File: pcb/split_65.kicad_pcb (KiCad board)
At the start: 2 copper layers, 375 x 105.4 mm, 333 parts, among them J1 PJ-3200B-4A, J10 AVR-ISP-6, J11 Breakaway_Tabs, J12 Breakaway_Tabs, J13 Breakaway_Tabs, J14 Breakaway_Tabs, J15 Breakaway_Tabs, J16 Breakaway_Tabs, J2 AVR-ISP-6, J3 Breakaway_Tabs, J4 Breakaway_Tabs, J5 Breakaway_Tabs, J6 Breakaway_Tabs, J7 Breakaway_Tabs, J8 Breakaway_Tabs, J9 PJ-3200B-4A, Q1 2N7002, Q2 2N7002, SW1 SW_Push, SW2 SW_Push, U1 ATmega32U4-AU, U2 PRTR5V0U2X, U3 ATmega32U4-AU, U4 PRTR5V0U2X, Y1 16MHz, Y2 16MHz

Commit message: moved usb/trrs port closer in
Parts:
- moved USB1 2.08 mm to (61.9, 44.4)
- moved USB2 2.08 mm to (340.5, 44.4)
- moved J1 2.08 mm to (138.1, 46.1)
- moved J9 2.08 mm to (264.3, 46.1)
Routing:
- net GND: track 71.9 -> 47.2 mm
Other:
- board size 375 x 105.4 mm -> 375 x 103.3 mm

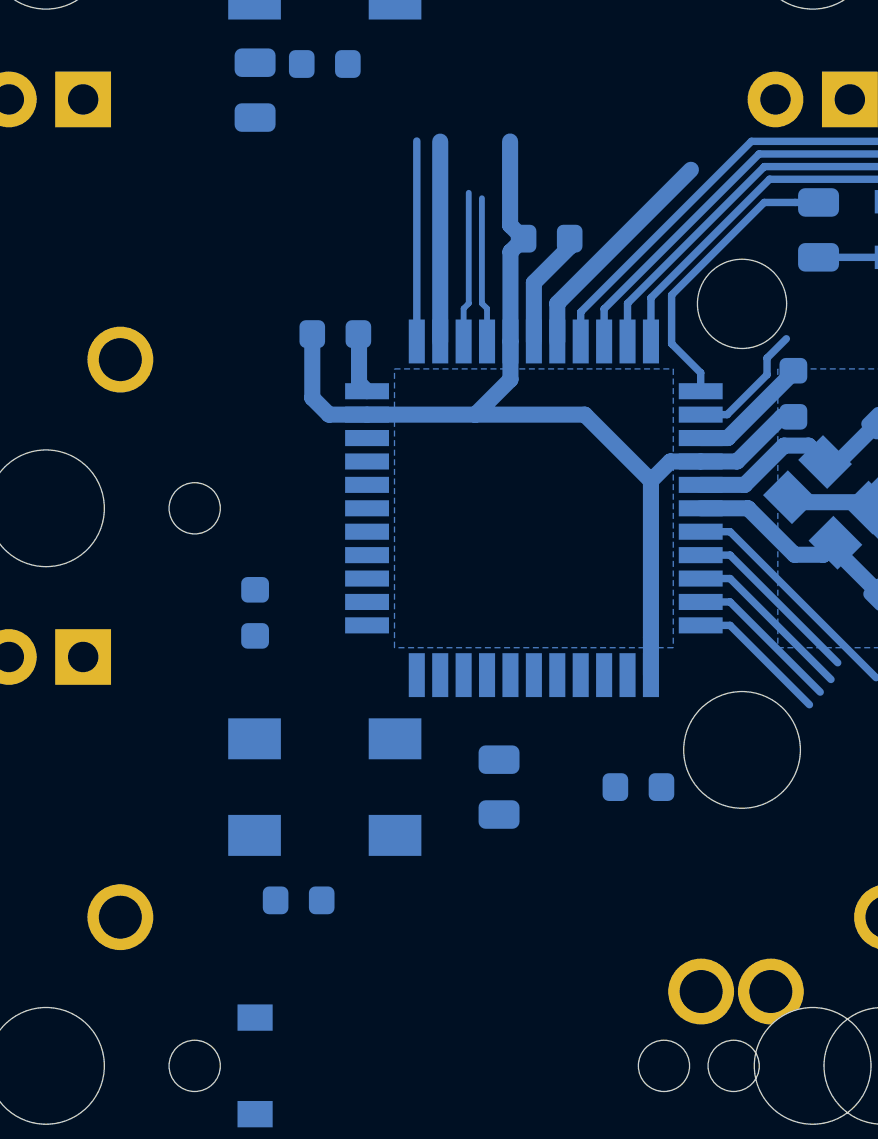
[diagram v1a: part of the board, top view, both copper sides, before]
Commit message: break out mcu pins
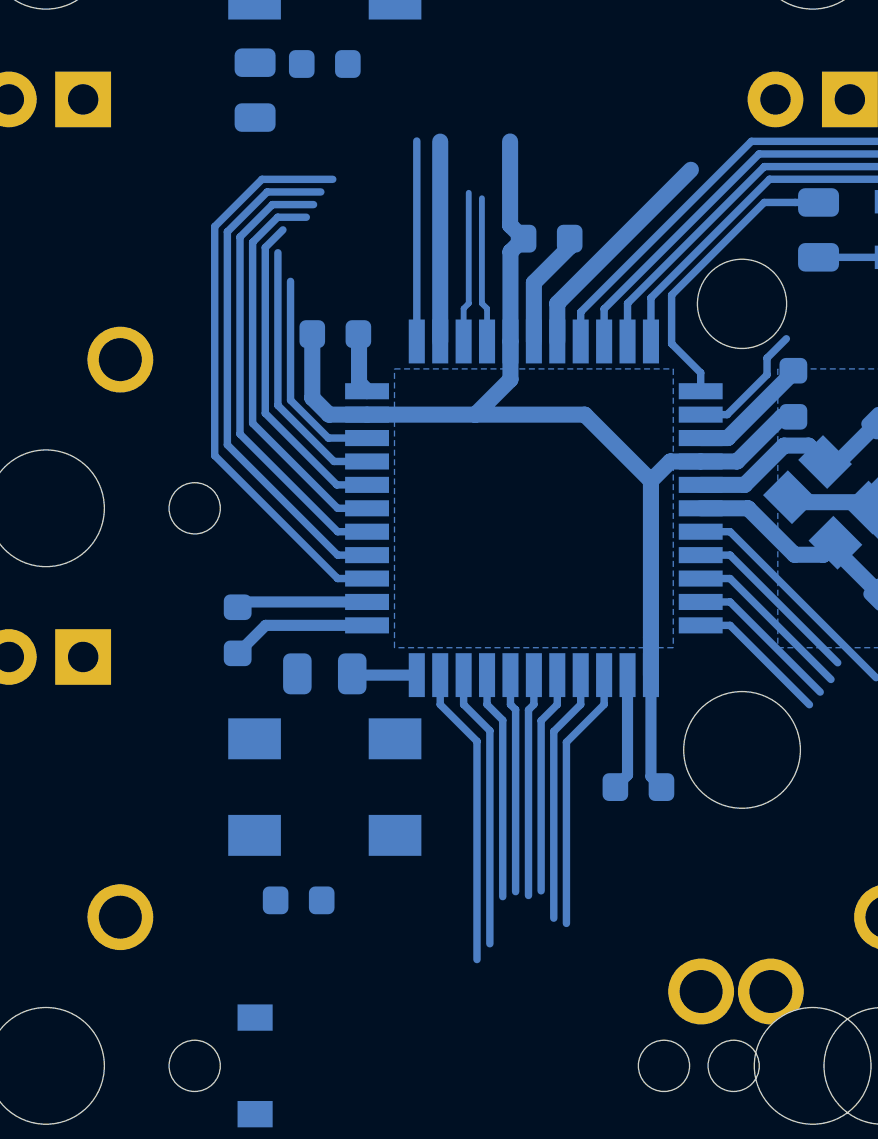
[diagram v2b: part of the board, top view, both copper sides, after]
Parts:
- moved R24 7.10 mm to (38.1, 124.7), turned to 0 degrees
- moved C6 0.84 mm to (35.1, 123.2)
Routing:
- net ROW0: track 0.00 -> 19.5 mm
- net ROW1: track 0.00 -> 17.4 mm
- net ROW2: track 0.00 -> 15.4 mm
- net ROW3: track 0.00 -> 13.5 mm
- net COL5: track 0.00 -> 11.0 mm
- net COL0: track 0.00 -> 10.2 mm
- net Net-(U1-Pad31): track 0.00 -> 9.55 mm
- net COL6: track 0.00 -> 9.05 mm
- net COL4: track 0.00 -> 9.02 mm
- net +5V: track 6.23 -> 15.0 mm
- net COL3: track 0.00 -> 8.69 mm
- net GND: track 47.2 -> 55.7 mm
- net Net-(U1-Pad30): track 0.00 -> 7.79 mm
- net COL1: track 0.00 -> 7.60 mm
- net COL2: track 0.00 -> 7.60 mm
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
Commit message: added more renders, changed pcb layout
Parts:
- added R91: 470, Resistor_SMD:R_0805_2012Metric, F.Cu at (168.0, -12.5)
- added R92: 470, Resistor_SMD:R_0805_2012Metric, F.Cu at (169.3, -14.8)
- C1, C10, C11, C12, C13, C14, C15, C16, C17, C18, C19, C2, C20, C21, C22, C23, C24, C25, C26, C27, C28, C29, C3, C30, C4, C5, C6, C7, C8, C9, D0, D1, D10, D11, D12, D13, D14, D15, D16, D17, D18, D19, D2, D20, D21, D22, D23, D24, D25, D26, D27, D28, D29, D3, D30, D31, D32, D33, D34, D35, D36, D37, D38, D39, D4, D40, D41, D42, D43, D44, D45, D46, D47, D48, D49, D5, D50, D51, D52, D53, D54, D55, D56, D57, D58, D59, D6, D60, D61, D62, D63, D64, D65, D66, D67, D68, D69, D7, D70, D71, D72, D73, D74, D75, D76, D8, D9, F1, F2, FID1, FID2, FID3, FID4, FID5, FID6, J10, J11, J12, J13, J14, J15, J16, J2, J3, J4, J5, J6, J7, J8, Q1, Q2, R0, R1, R10, R11, R12, R13, R14, R15, R16, R17, R18, R19, R2, R20, R21, R22, R23, R24, R25, R26, R27, R28, R29, R3, R30, R31, R32, R33, R34, R35, R36, R37, R38, R39, R4, R40, R41, R42, R43, R44, R45, R46, R47, R48, R49, R5, R50, R51, R52, R53, R54, R55, R56, R57, R58, R59, R6, R60, R61, R62, R63, R64, R65, R66, R67, R68, R69, R7, R70, R71, R72, R73, R74, R75, R76, R77, R78, R79, R8, R80, R81, R82, R83, R84, R85, R86, R87, R88, R89, R9, R90, SW1, SW2, U1, U2, U3, U4, Y1, Y2: moved to F.Cu
- LED1, LED10, LED11, LED12, LED13, LED14, LED15, LED16, LED2, LED3, LED4, LED5, LED6, LED7, LED8, LED9: value VAL** -> WS2812B; moved to F.Cu
- MX0, MX1, MX10, MX11, MX12, MX13, MX14, MX15, MX18, MX19, MX2, MX20, MX21, MX22, MX23, MX25, MX26, MX27, MX28, MX29, MX3, MX30, MX38, MX39, MX4, MX40, MX41, MX42, MX43, MX44, MX46, MX47, MX48, MX49, MX5, MX50, MX51, MX52, MX53, MX54, MX56, MX57, MX58, MX59, MX6, MX60, MX61, MX62, MX64, MX65, MX66, MX67, MX68, MX69, MX7, MX71, MX72, MX8, MX80, MX81, MX82: value 1U -> MXOnly-1U
- MX31: footprint MX_Alps_Hybrid:MXOnly-1.5U-FLIPPED -> MX_Alps_Hybrid:MXOnly-1U
- MX33, MX35: footprint MX_Alps_Hybrid:MXOnly-1.25U -> MX_Alps_Hybrid:MXOnly-1.25U-FLIPPED
- MX34: footprint MX_Alps_Hybrid:MXOnly-1.5U -> MX_Alps_Hybrid:MXOnly-1.25U
- moved J13 420.1 mm to (54.9, -96.0), turned to 0 degrees
- moved R89 418.4 mm to (298.0, -141.3), turned to 0 degrees
- moved J3 414.0 mm to (11.9, -11.7), turned to 0 degrees
- moved J7 404.6 mm to (17.7, -11.7), turned to 0 degrees
- moved J14 400.5 mm to (11.9, -12.6), turned to 0 degrees
- moved J8 399.4 mm to (17.7, -10.8), turned to 0 degrees
- moved J12 389.6 mm to (11.9, -10.8), turned to 0 degrees
- moved SW2 389.1 mm to (13.2, -15.9), turned to 0 degrees
- moved J11 385.5 mm to (23.6, -10.7), turned to 0 degrees
- moved D22 377.8 mm to (293.9, -142.6), turned to 0 degrees
- moved J15 372.6 mm to (66.6, -96.0), turned to 0 degrees
- moved J16 372.6 mm to (60.7, -96.0), turned to 0 degrees
- moved R40 371.8 mm to (263.3, -99.3), turned to 0 degrees
- moved C30 370.0 mm to (38.0, -11.2), turned to 0 degrees
- moved C29 356.9 mm to (41.0, -11.2), turned to 0 degrees
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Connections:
- LED1 pad 4: RGBLED -> Net-(LED1-Pad4)
- LED9 pad 4: RGBLED-R -> Net-(LED9-Pad4)
- MX16 pad 3: +5V -> CAPSLOCK
- MX17 pad 3: +5V -> CAPSLOCK
- MX31 pad 1: COL1 -> COL3
- MX31 pad 2: Net-(D30-Pad2) -> Net-(D31-Pad2)
- MX32 pad 4: Net-(MX31-Pad4) -> Net-(MX32-Pad4)
- MX33 pad 4: Net-(MX33-Pad4) -> Net-(MX31-Pad4)
- R33 pad 2: Net-(MX31-Pad4) -> Net-(MX32-Pad4)
- R34 pad 2: Net-(MX33-Pad4) -> Net-(MX31-Pad4)
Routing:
- net GND: track 55.7 -> 0.00 mm
- net Net-(U1-Pad8): track 20.0 -> 0.00 mm
- net ROW0: track 19.5 -> 0.00 mm
- net SCK: track 18.1 -> 0.00 mm
- net ROW1: track 17.4 -> 0.00 mm
- net MOSI: track 16.9 -> 0.00 mm
- net MISO: track 15.6 -> 0.00 mm
- net ROW2: track 15.4 -> 0.00 mm
- net +5V: track 15.0 -> 0.00 mm
- net VBUS: track 14.6 -> 0.00 mm
- net ROW3: track 13.5 -> 0.00 mm
- net COL5: track 11.0 -> 0.00 mm
- net COL0: track 10.2 -> 0.00 mm
- net LEDPWM: track 10.0 -> 0.00 mm
- net Net-(U1-Pad31): track 9.55 -> 0.00 mm
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
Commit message: reset layouts
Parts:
- C1, C10, C11, C12, C13, C14, C15, C16, C17, C18, C19, C2, C20, C21, C22, C23, C24, C25, C26, C27, C28, C29, C3, C30, C4, C5, C6, C7, C8, C9, D0, D1, D10, D11, D12, D13, D14, D15, D16, D17, D18, D19, D2, D20, D21, D22, D23, D24, D25, D26, D27, D28, D29, D3, D30, D31, D32, D33, D34, D35, D36, D37, D38, D39, D4, D40, D41, D42, D43, D44, D45, D46, D47, D48, D49, D5, D50, D51, D52, D53, D54, D55, D56, D57, D58, D59, D6, D60, D61, D62, D63, D64, D65, D66, D67, D68, D69, D7, D70, D71, D72, D73, D74, D75, D76, D8, D9, F1, F2, FID1, FID2, FID3, FID4, FID5, FID6, J10, J11, J12, J13, J14, J15, J16, J2, J3, J4, J5, J6, J7, J8, LED1, LED10, LED11, LED12, LED13, LED14, LED15, LED16, LED2, LED3, LED4, LED5, LED6, LED7, LED8, LED9, Q1, Q2, R0, R1, R10, R11, R12, R13, R14, R15, R16, R17, R18, R19, R2, R20, R21, R22, R23, R24, R25, R26, R27, R28, R29, R3, R30, R31, R32, R33, R34, R35, R36, R37, R38, R39, R4, R40, R41, R42, R43, R44, R45, R46, R47, R48, R49, R5, R50, R51, R52, R53, R54, R55, R56, R57, R58, R59, R6, R60, R61, R62, R63, R64, R65, R66, R67, R68, R69, R7, R70, R71, R72, R73, R74, R75, R76, R77, R78, R79, R8, R80, R81, R82, R83, R84, R85, R86, R87, R88, R89, R9, R90, R91, R92, SW1, SW2, U1, U2, U3, U4, Y1, Y2: moved to B.Cu
- moved U3 352.3 mm to (351.5, 215.2)
- moved U1 317.7 mm to (45.2, 119.1), turned to 270 degrees
- moved Y1 234.8 mm to (55.4, 118.9), turned to 135 degrees
- moved J11 203.4 mm to (42.6, -213.2)
- moved J12 203.2 mm to (30.9, -213.1)
- moved J8 203.2 mm to (36.8, -213.1)
- moved C11 202.5 mm to (193.3, -212.7)
- moved C19 202.5 mm to (190.3, -212.7)
- moved C10 202.3 mm to (105.2, -212.6)
- moved C12 202.3 mm to (111.3, -212.6)
- moved C13 202.3 mm to (84.2, -212.6)
- moved C14 202.3 mm to (117.3, -212.6)
- moved C15 202.3 mm to (120.3, -212.6)
- moved C16 202.3 mm to (123.3, -212.6)
- moved C17 202.3 mm to (126.3, -212.6)
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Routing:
- net GND: track 0.00 -> 35.5 mm
- net Net-(C1-Pad1): track 0.00 -> 7.79 mm
- net Net-(C2-Pad1): track 0.00 -> 7.43 mm

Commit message: laid out ws2812b
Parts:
- moved LED9 427.8 mm to (378.6, 128.6), turned to 90 degrees
- moved LED10 422.0 mm to (311.9, 128.6), turned to 90 degrees
- moved LED16 412.4 mm to (378.6, 100.0), turned to 90 degrees
- moved LED15 395.2 mm to (378.6, 71.4), turned to 90 degrees
- moved LED11 375.9 mm to (245.3, 128.6), turned to 90 degrees
- moved LED14 354.5 mm to (311.9, 71.4), turned to 90 degrees
- moved LED1 350.0 mm to (38.1, 128.6), turned to 90 degrees
- moved LED12 345.9 mm to (240.5, 100.0), turned to 90 degrees
- moved LED2 338.8 mm to (92.9, 128.6), turned to 90 degrees
- moved LED3 336.3 mm to (147.6, 128.6), turned to 90 degrees
- moved LED13 320.5 mm to (245.3, 71.4), turned to 90 degrees
- moved LED4 310.2 mm to (152.4, 100.0), turned to 90 degrees
- moved LED8 310.1 mm to (38.1, 100.0), turned to 90 degrees
- moved LED5 289.6 mm to (147.6, 71.4), turned to 90 degrees
- moved LED7 281.1 mm to (38.1, 71.4), turned to 90 degrees
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
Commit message: removed underglow and backlight, routed left hand
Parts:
- removed C15, C16, C17, C18, C19, C20, C21, C22, C23, C24, C25, C26, C27, C28, C29, C30: 0.1uF, Capacitor_SMD:C_0603_1608Metric
- removed LED1, LED10, LED11, LED12, LED13, LED14, LED15, LED16, LED2, LED3, LED4, LED5, LED6, LED7, LED8, LED9: WS2812B, WS2812B:WS2812B
- removed Q1, Q2: 2N7002, Package_TO_SOT_SMD:SOT-23
- removed R0, R1, R10, R11, R12, R13, R14, R15, R16, R17, R19, R2, R20, R21, R22, R23, R25, R26, R27, R28, R29, R3, R30, R31, R32, R33, R34, R35, R36, R4, R43, R44, R45, R46, R47, R48, R49, R5, R50, R51, R52, R53, R54, R55, R56, R57, R58, R59, R6, R60, R61, R62, R63, R64, R65, R66, R67, R68, R7, R70, R71, R72, R73, R74, R75, R76, R77, R78, R79, R80, R81, R82, R83, R84, R91, R92: 470, Resistor_SMD:R_0805_2012Metric
- removed R37, R85: 1k, Resistor_SMD:R_0805_2012Metric
- removed SW1, SW2: SW_Push, locallib:SKQGADE010
- added G***: LOGO, AIRI_Logo:airi_icon-7.6, B.Cu at (45.2, 119.1)
- added G***: LOGO, AIRI_Logo:airi_icon-7.6, B.Cu at (329.8, 125.6)
- MX0, MX1, MX10, MX11, MX12, MX13, MX14, MX15, MX18, MX19, MX2, MX20, MX21, MX22, MX23, MX25, MX26, MX27, MX28, MX29, MX3, MX30, MX31, MX38, MX39, MX4, MX40, MX41, MX42, MX43, MX44, MX46, MX47, MX48, MX49, MX5, MX50, MX51, MX52, MX53, MX54, MX56, MX57, MX58, MX59, MX6, MX60, MX61, MX62, MX64, MX65, MX66, MX67, MX68, MX69, MX7, MX71, MX72, MX8, MX80, MX81, MX82: value MXOnly-1U -> MXOnly-1U-NoLED; footprint MX_Alps_Hybrid:MXOnly-1U -> MX_Alps_Hybrid:MXOnly-1U-NoLED
- MX16, MX17: value MXOnly-1U -> MXOnly-1U-NoLED
- MX24, MX63, MX74: value MXOnly-1U -> MXOnly-1U-NoLED; footprint MX_Alps_Hybrid:MXOnly-2.25U -> MX_Alps_Hybrid:MXOnly-2.25U-NoLED
- MX32, MX34, MX75, MX77: value MXOnly-1U -> MXOnly-1U-NoLED; footprint MX_Alps_Hybrid:MXOnly-1.25U -> MX_Alps_Hybrid:MXOnly-1.25U-NoLED
- MX33, MX35, MX79: value MXOnly-1U -> MXOnly-1U-NoLED; footprint MX_Alps_Hybrid:MXOnly-1.25U-FLIPPED -> MX_Alps_Hybrid:MXOnly-1.25U-NoLED
- MX36, MX73: value MXOnly-1U -> MXOnly-1U-NoLED; footprint MX_Alps_Hybrid:MXOnly-3U -> MX_Alps_Hybrid:MXOnly-3U-NoLED
- MX37: value MXOnly-1U -> MXOnly-1U-NoLED; footprint MX_Alps_Hybrid:MXOnly-2.75U-FLIPPED -> MX_Alps_Hybrid:MXOnly-2.75U-NoLED
- MX45: value MXOnly-1U -> MXOnly-1U-NoLED; footprint MX_Alps_Hybrid:MXOnly-2U -> MX_Alps_Hybrid:MXOnly-2U-NoLED
- MX55, MX76, MX78, MX9: value MXOnly-1U -> MXOnly-1U-NoLED; footprint MX_Alps_Hybrid:MXOnly-1.5U -> MX_Alps_Hybrid:MXOnly-1.5U-NoLED
- MX70: value MXOnly-1U -> MXOnly-1U-NoLED; footprint MX_Alps_Hybrid:MXOnly-1.75U -> MX_Alps_Hybrid:MXOnly-1.75U-NoLED
- moved C10 474.8 mm to (170.1, 257.7)
- moved C11 474.8 mm to (258.2, 257.6)
- moved C12 474.8 mm to (176.2, 257.7)
- moved C13 474.8 mm to (149.1, 257.7)
- moved C14 474.8 mm to (182.2, 257.7)
- moved C8 474.8 mm to (164.1, 257.7)
- moved C9 474.8 mm to (167.1, 257.7)
- moved D76 474.8 mm to (234.9, 262.8)
- moved FID4 474.8 mm to (263.3, 261.5)
- moved J11 474.8 mm to (107.5, 257.1)
- moved J12 474.8 mm to (95.8, 257.2)
- moved J14 474.8 mm to (95.8, 259.0)
- moved J3 474.8 mm to (95.8, 258.1)
- moved J6 474.8 mm to (101.7, 259.0)
- moved J7 474.8 mm to (101.7, 258.1)
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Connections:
- R18 pad 1: LEDGND -> Net-(MX16-Pad4)
- R18 pad 2: Net-(MX16-Pad4) -> GND
- U1 pad 12: LEDPWM -> Net-(U1-Pad12)
- U1 pad 20: Net-(U1-Pad20) -> COL6
- U1 pad 21: ROW4 -> COL7
- U1 pad 25: COL4 -> COL5
- U1 pad 26: COL3 -> COL4
- U1 pad 27: COL2 -> COL3
- U1 pad 28: COL1 -> COL2
- U1 pad 29: Net-(U1-Pad29) -> COL1
- U1 pad 30: Net-(U1-Pad30) -> ROW4
- U1 pad 31: Net-(U1-Pad31) -> COL0
- U1 pad 32: COL0 -> ROW3
- U1 pad 36: ROW0 -> Net-(U1-Pad36)
- U1 pad 37: ROW1 -> Net-(U1-Pad37)
- U1 pad 38: ROW2 -> Net-(U1-Pad38)
- U1 pad 39: ROW3 -> ROW0
- U1 pad 40: COL5 -> ROW1
- U1 pad 41: COL6 -> ROW2
- U1 pad 8: Net-(U1-Pad8) -> CAPSLOCK
- U3 pad 12: LEDPWM-R -> Net-(U3-Pad12)
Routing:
- net +5V: track 0.00 -> 254.5 mm, vias 0 -> 8
- net GND: track 35.5 -> 231.9 mm, vias 0 -> 1
- net ROW0: track 0.00 -> 193.3 mm, vias 0 -> 4
- net COL7: track 0.00 -> 192.0 mm
- net COL5: track 0.00 -> 189.2 mm
- net COL6: track 0.00 -> 180.5 mm
- net ROW1: track 0.00 -> 161.9 mm, vias 0 -> 4
- net SCL: track 0.00 -> 159.5 mm, vias 0 -> 2
- net ROW3: track 0.00 -> 155.4 mm, vias 0 -> 4
- net COL4: track 0.00 -> 154.8 mm
- net SDA: track 0.00 -> 148.7 mm
- net ROW2: track 0.00 -> 143.6 mm, vias 0 -> 4
- net COL3: track 0.00 -> 137.9 mm
- net ROW4: track 0.00 -> 132.9 mm
- net COL1: track 0.00 -> 106.5 mm
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- added copper zone on B.Cu, net GNDA

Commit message: routed right hand side
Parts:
- moved C9 221.3 mm to (343.0, 123.4), turned to 315 degrees
- moved R90 221.2 mm to (336.4, 57.2), turned to 90 degrees
- moved C8 220.9 mm to (343.2, 128.4), turned to 45 degrees
- moved R89 219.2 mm to (344.7, 56.0), turned to 90 degrees
- moved C13 214.7 mm to (321.5, 129.8), turned to 90 degrees
- moved D76 214.4 mm to (330.4, 70.8), turned to 45 degrees
- moved C10 212.8 mm to (329.8, 116.9), turned to 90 degrees
- moved C12 200.4 mm to (333.8, 133.9)
- moved C14 194.4 mm to (321.5, 122.0), turned to 270 degrees
- moved R88 161.5 mm to (337.5, 132.8), turned to 90 degrees
- moved C11 158.5 mm to (339.8, 121.7), turned to 225 degrees
- moved F2 153.8 mm to (335.8, 68.5)
- moved Y2 120.2 mm to (340.7, 125.7), turned to 135 degrees
- moved R69 114.8 mm to (323.3, 135.7)
- moved D41 19.1 mm to (354.2, 67.3), turned to 180 degrees
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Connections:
- U3 pad 1: ROW4-R -> ROW0-R
- U3 pad 20: Net-(U3-Pad20) -> COL8-R
- U3 pad 21: Net-(U3-Pad21) -> COL7-R
- U3 pad 25: COL0-R -> COL5-R
- U3 pad 26: COL1-R -> COL6-R
- U3 pad 27: ROW3-R -> ROW4-R
- U3 pad 28: ROW2-R -> COL0-R
- U3 pad 29: ROW1-R -> COL1-R
- U3 pad 30: ROW0-R -> COL2-R
- U3 pad 31: COL6-R -> COL3-R
- U3 pad 32: Net-(U3-Pad32) -> COL4-R
- U3 pad 36: Net-(U3-Pad36) -> ROW3-R
- U3 pad 38: COL5-R -> Net-(U3-Pad38)
- U3 pad 39: COL4-R -> Net-(U3-Pad39)
- U3 pad 40: COL2-R -> ROW2-R
- U3 pad 41: COL3-R -> ROW1-R
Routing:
- net +5VA: track 0.00 -> 279.5 mm, vias 0 -> 5
- net ROW0-R: track 0.00 -> 206.8 mm, vias 0 -> 2
- net COL0-R: track 0.00 -> 206.4 mm
- net GNDA: track 60.8 -> 265.2 mm, vias 0 -> 1
- net COL1-R: track 0.00 -> 202.9 mm
- net ROW1-R: track 0.00 -> 201.6 mm, vias 0 -> 2
- net ROW3-R: track 0.00 -> 176.7 mm, vias 0 -> 2
- net ROW2-R: track 0.00 -> 174.6 mm, vias 0 -> 2
- net SCL-R: track 0.00 -> 162.7 mm, vias 0 -> 3
- net SDA-R: track 0.00 -> 160.4 mm, vias 0 -> 3
- net COL2-R: track 0.00 -> 159.7 mm
- net COL3-R: track 0.00 -> 150.4 mm
- net ROW4-R: track 0.00 -> 142.5 mm, vias 0 -> 4
- net COL8-R: track 0.00 -> 132.5 mm
- net COL7-R: track 0.00 -> 131.9 mm
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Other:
- board text added: "jtallbean"

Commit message: added step files, combined and panelized
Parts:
- removed J15, J16: Breakaway_Tabs, locallib:breakaway-mousebites
- FID2, FID4, FID6: moved to F.Cu
- moved FID2 351.7 mm to (23.8, 38.7)
- moved FID1 314.8 mm to (23.8, 38.7)
- moved J12 309.3 mm to (328.6, 53.6)
- moved J13 256.7 mm to (328.6, 145.9)
- moved FID6 251.5 mm to (23.8, 157.8)
- moved J11 249.8 mm to (252.4, 53.6)
- moved FID5 246.1 mm to (23.8, 157.8)
- moved FID4 236.6 mm to (342.9, 38.7)
- moved J8 224.1 mm to (195.3, 53.6)
- moved J7 212.0 mm to (157.2, 53.6)
- moved J6 205.5 mm to (100.0, 53.6)
- moved FID3 179.5 mm to (342.9, 38.7)
- moved J5 172.7 mm to (38.1, 53.6)
- moved J14 170.9 mm to (223.8, 145.9)
- moved J3 126.2 mm to (38.1, 145.9)
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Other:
- board size 375 x 103.3 mm -> 325 x 125 mm
